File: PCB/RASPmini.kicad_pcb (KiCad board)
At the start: 2 copper layers, 65 x 56 mm, 14 parts, among them P0 Raspberry PI GPIO, P1 MPU9250, P2 MS5611, P3 PCA9685, P5 UART, P6 RC IN

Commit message: 添加OSHWA logo
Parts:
- added G***: LOGO, Raspmini:OSHWA, B.Cu at (143.5, 64.8)

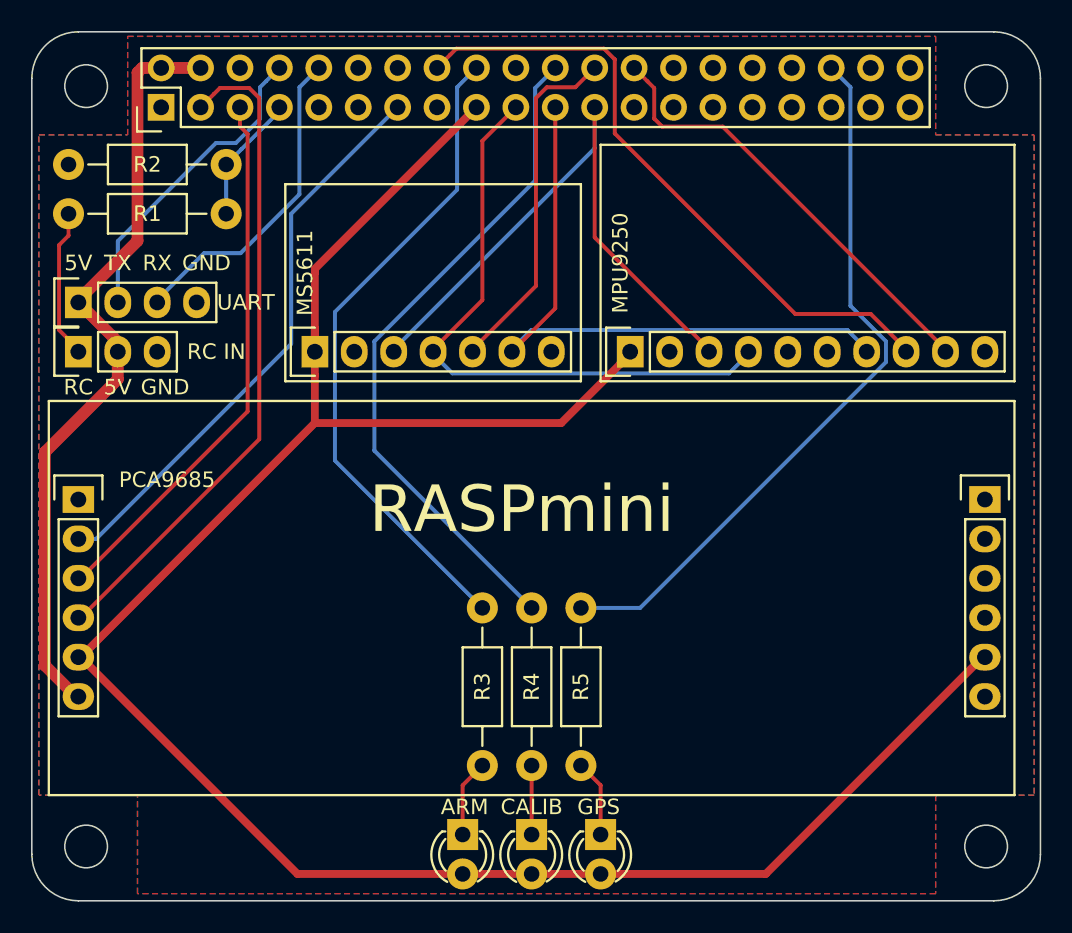
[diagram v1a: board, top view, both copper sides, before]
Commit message: 串口电源改为3.3v
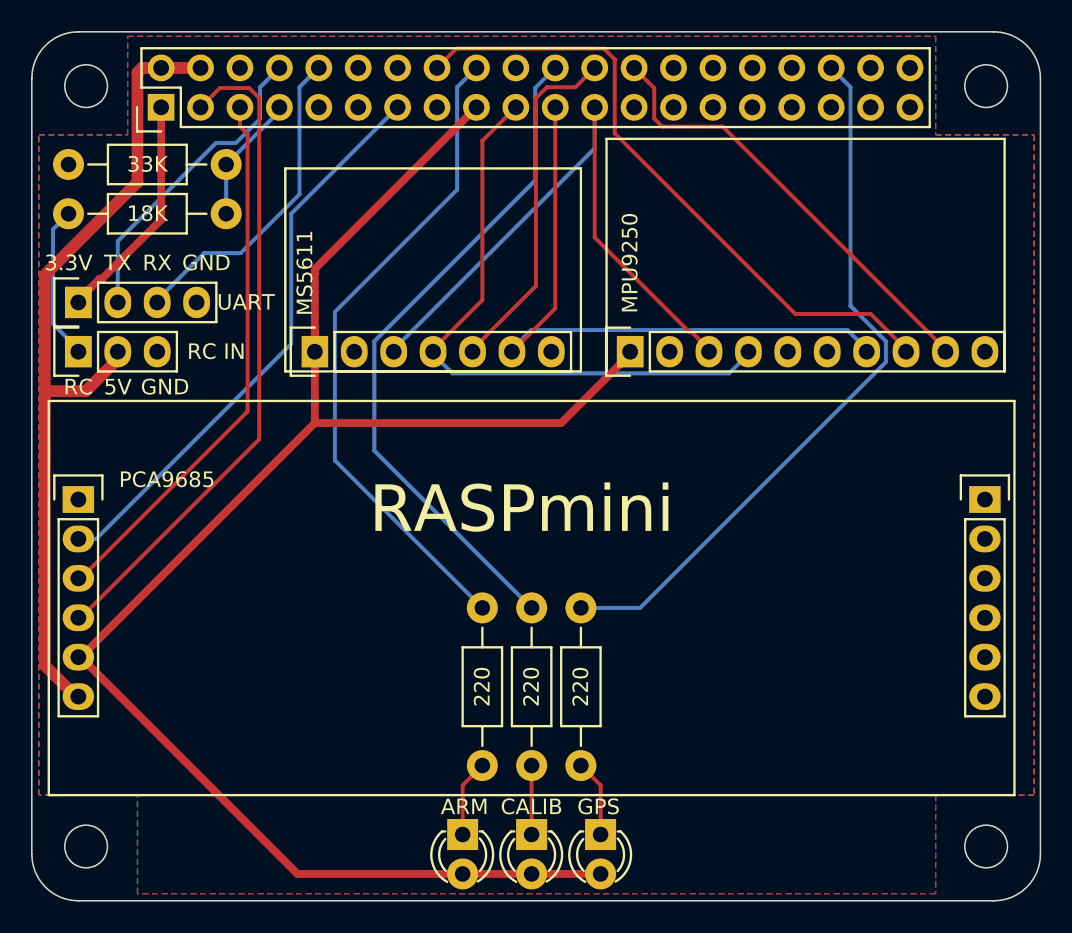
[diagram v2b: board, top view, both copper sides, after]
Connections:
- P5 pad 1: +5V -> +3V3
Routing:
- net +3V3: track 140.0 -> 124.3 mm
- net +5V: track 50.0 -> 53.9 mm
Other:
- board text added: "3.3V"
